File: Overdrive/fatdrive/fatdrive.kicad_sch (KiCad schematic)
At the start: 46 parts, among them J1 Conn_01x04_Pin, SW1 SW_SPDT, U1 TL072, U2 TL072, U3 4049

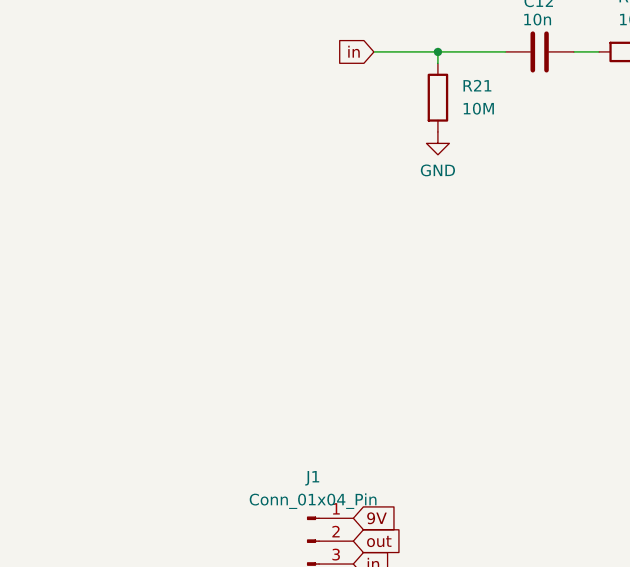
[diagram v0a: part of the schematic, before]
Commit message: updated readme, comments on fatdrive schematic
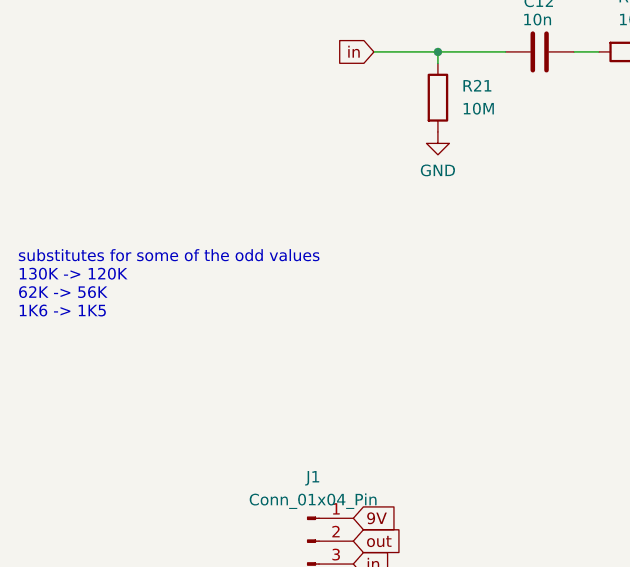
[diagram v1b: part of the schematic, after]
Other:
- note added: "substitutes for some of the odd values 130K -> 120K 62K -> 56K 1K6 -> 1K5"
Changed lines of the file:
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@@
     (stroke (width 0) (type default))
+  )
+  (text "substitutes for some of the odd values\n130K -> 120K\n62K -> 56K \n1K6 -> 1K5"
+    (at 15.4432 81.5848 0)
+    (effects (font (size 1.27 1.27)) (justify left bottom))
   )
   (text "tone\n" (at 175.768 123.825 0)
